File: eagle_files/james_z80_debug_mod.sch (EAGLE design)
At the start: 50 parts, among them IC1 74LS32N, IC10 74HC573N, IC11 27C128P, IC13 74LS245N, IC14 74LS245N, IC15 74LS245N, IC16 74HC125N, IC2 74LS04N, IC3 74LS139N, IC4 74HC573N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

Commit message: Update monitor mods.
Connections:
- net GND: now also IC9.14
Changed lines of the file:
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@@
 <description>Main Board</description>
 <plain>
-<text x="5.08" y="-58.42" size="1.27" layer="97">NC</text>
 <text x="-5.08" y="-78.74" size="1.27" layer="97" align="top-center">Ribbon cable DIL Header
 To BBC Micro
@@
 <wire x1="10.16" y1="-45.72" x2="15.24" y2="-45.72" width="0.1524" layer="91"/>
 <wire x1="15.24" y1="-45.72" x2="15.24" y2="-48.26" width="0.1524" layer="91"/>
-</segment>
-<segment>
+<pinref part="IC9" gate="G$1" pin="14"/>
+<wire x1="2.54" y1="-58.42" x2="10.16" y2="-58.42" width="0.1524" layer="91"/>
+<wire x1="10.16" y1="-58.42" x2="10.16" y2="-55.88" width="0.1524" layer="91"/>
+<junction x="10.16" y="-55.88"/>
+</segment>
+<segment>

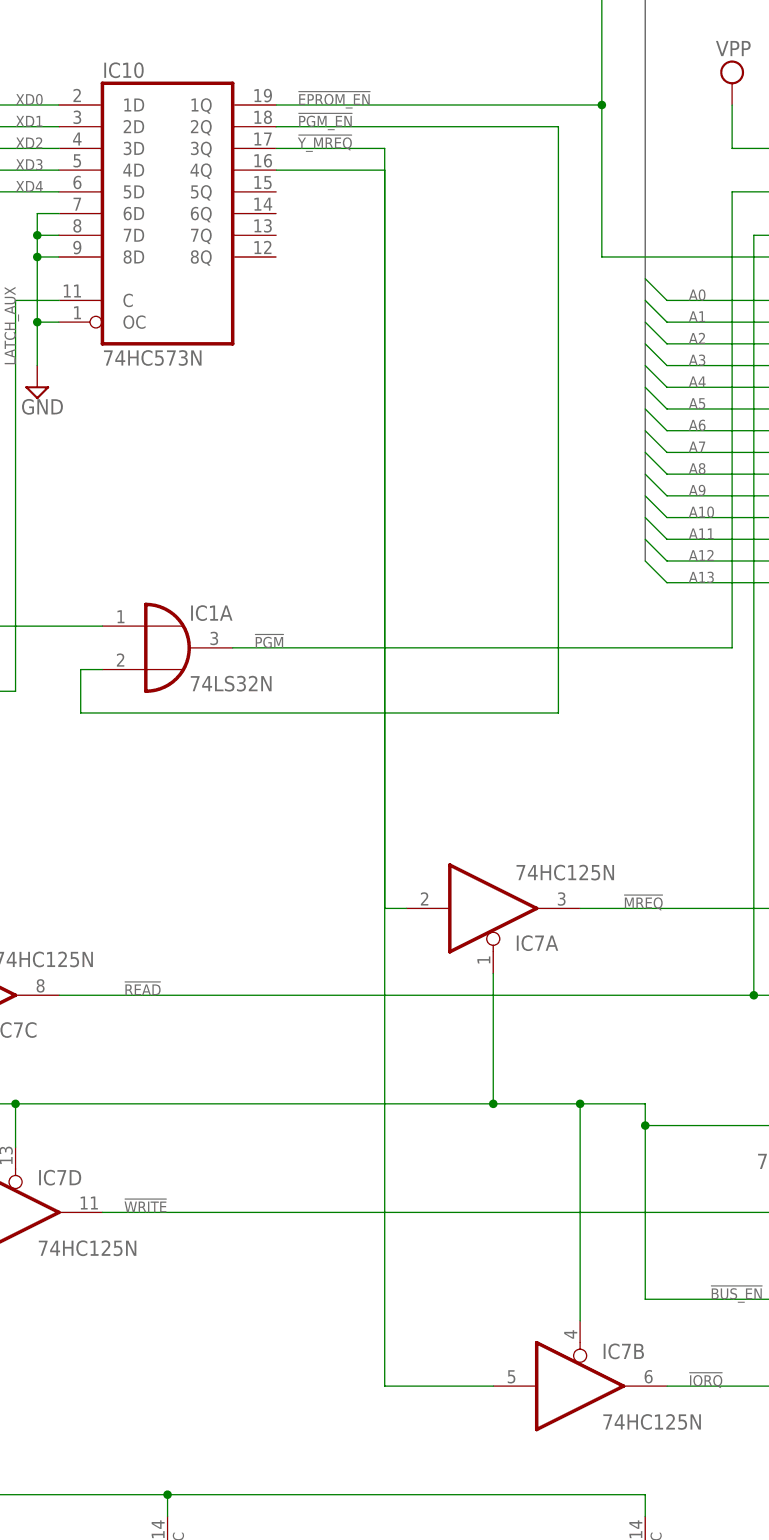
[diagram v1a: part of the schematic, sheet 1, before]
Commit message: Add a label to eagle schematics.
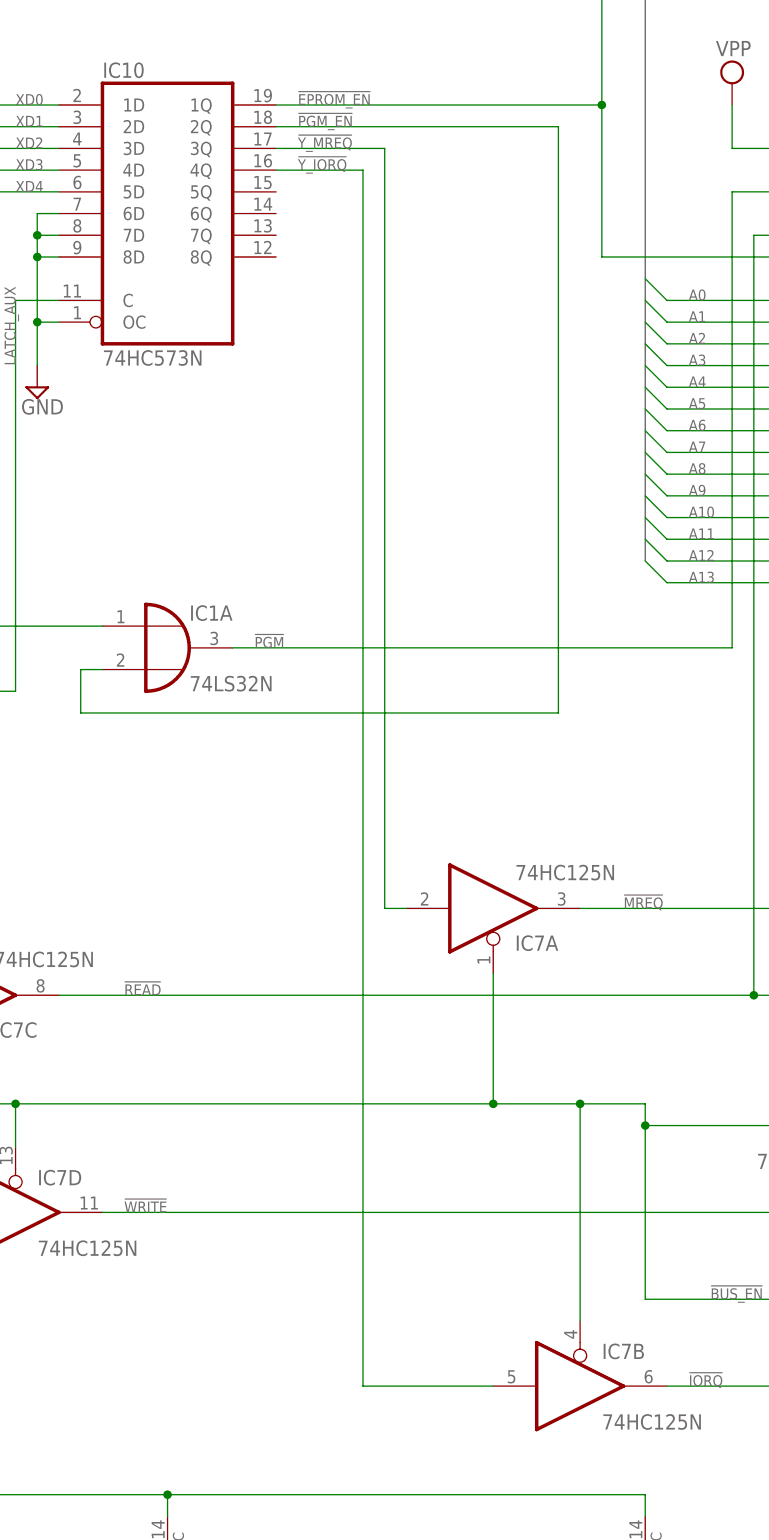
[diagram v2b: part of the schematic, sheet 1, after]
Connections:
- net N$4 renamed !Y_IORQ
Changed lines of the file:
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@@
 </segment>
 </net>
-<net name="N$4" class="0">
+<net name="!Y_IORQ" class="0">
 <segment>
 <pinref part="IC10" gate="A" pin="4Q"/>
-<wire x1="254" y1="-68.58" x2="266.7" y2="-68.58" width="0.1524" layer="91"/>
-<wire x1="266.7" y1="-68.58" x2="266.7" y2="-210.82" width="0.1524" layer="91"/>
+<wire x1="254" y1="-68.58" x2="264.16" y2="-68.58" width="0.1524" layer="91"/>
+<wire x1="264.16" y1="-68.58" x2="264.16" y2="-210.82" width="0.1524" layer="91"/>
 <pinref part="IC7" gate="B" pin="I"/>
-<wire x1="266.7" y1="-210.82" x2="279.4" y2="-210.82" width="0.1524" layer="91"/>
+<wire x1="264.16" y1="-210.82" x2="279.4" y2="-210.82" width="0.1524" layer="91"/>
+<label x="256.54" y="-68.58" size="1.27" layer="95"/>
 </segment>
 </net>
